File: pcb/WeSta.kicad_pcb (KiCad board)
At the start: 2 copper layers, 30 x 90 mm, 20 parts, among them J2 Conn_01x02, J3 RG-9/11/15, U1 ESP32-C3-MINI-1, U2 AW32001ECSR, U3 BH1730FVC, U4 BME280

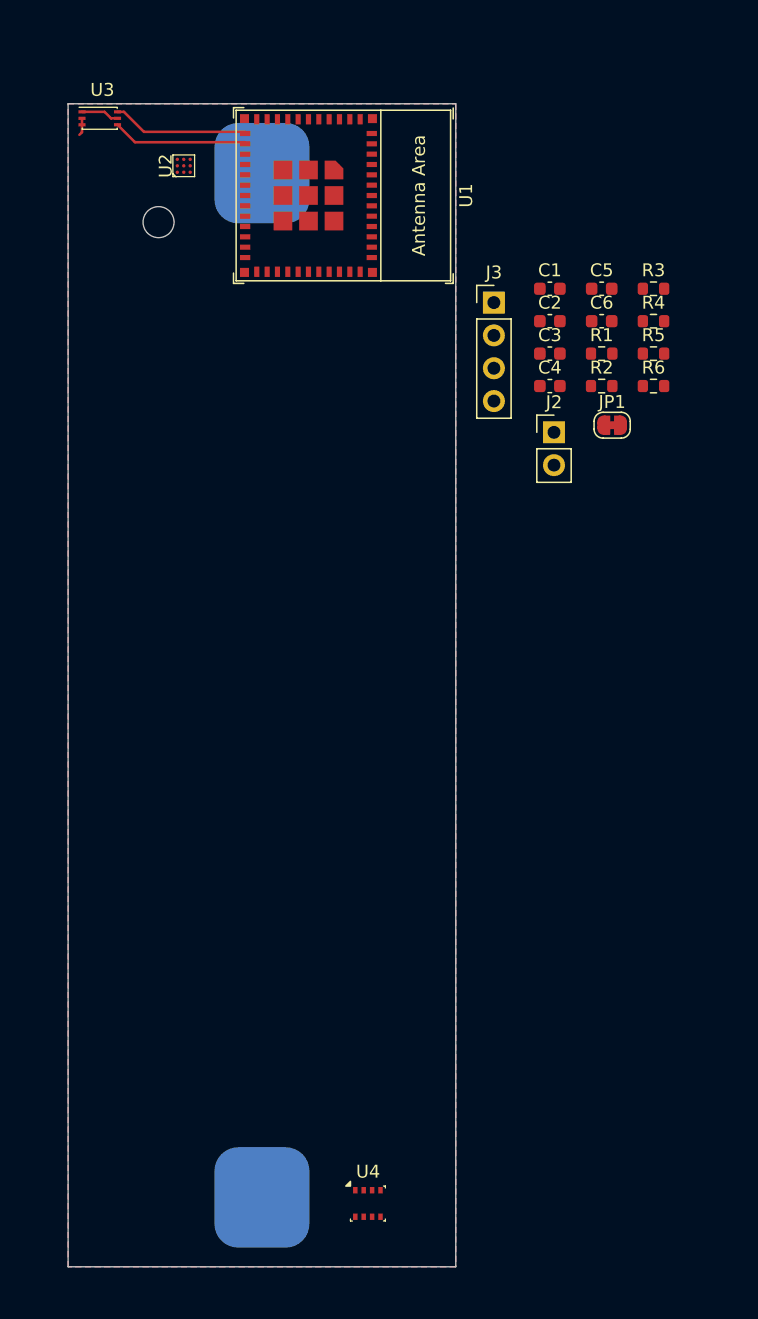
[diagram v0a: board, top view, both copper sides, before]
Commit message: Finalize rough PCB version
- Split sensors into own sub schematic as well as sub-sub sensor schematics
- Split piwer into own sub schematic
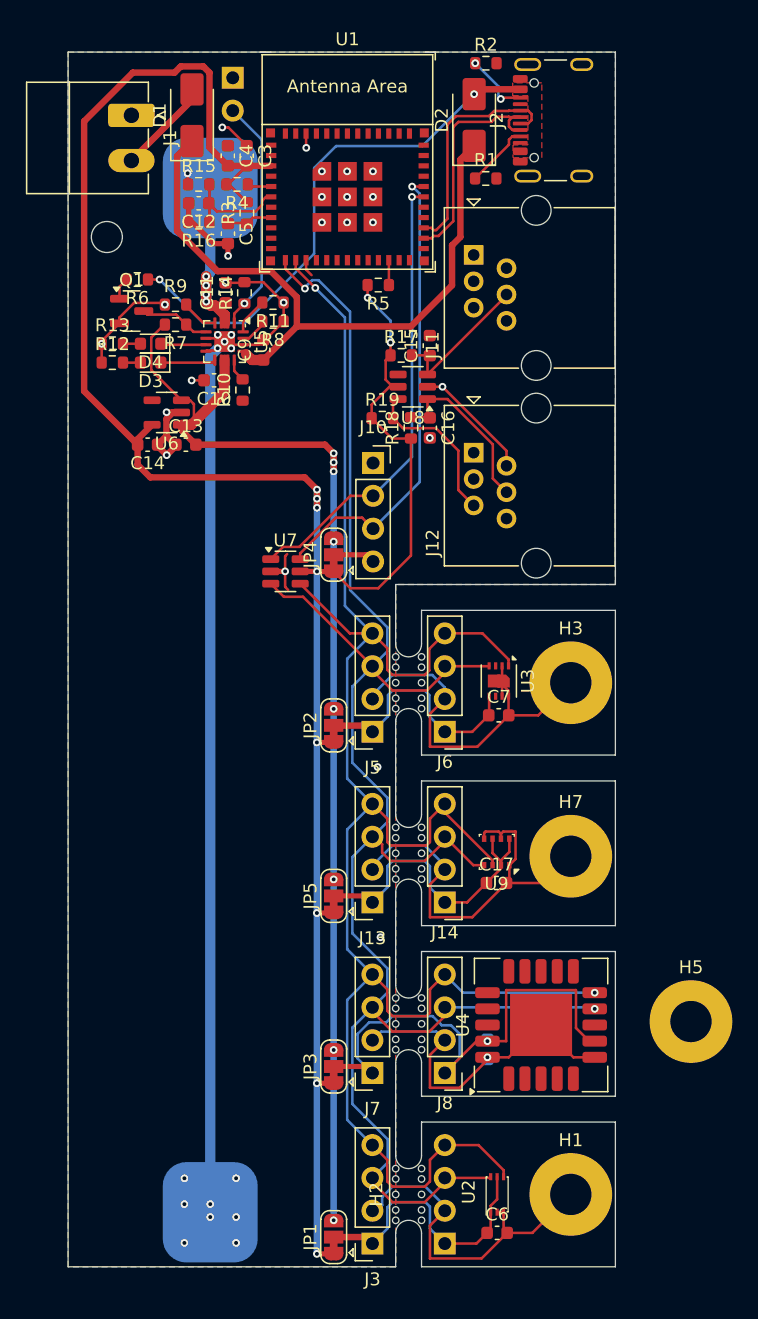
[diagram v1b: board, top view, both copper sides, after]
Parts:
- removed the C4 at (37.3, 21.8)
- removed the R4 at (45.3, 16.8)
- removed the R5 at (45.3, 19.3)
- added C10: 20u, Capacitor_SMD:C_0603_1608Metric, F.Cu at (11.3, 21.4)
- added C12: 100n, Capacitor_SMD:C_0603_1608Metric, F.Cu at (10.1, 7.70)
- added C13: 20u, Capacitor_SMD:C_0603_1608Metric, F.Cu at (9.12, 26.4)
- added C14: 20u, Capacitor_SMD:C_0603_1608Metric, F.Cu at (6.16, 26.4)
- added C15: 10p, Capacitor_SMD:C_0603_1608Metric, F.Cu at (28.0, 18.7)
- added C16: 10p, Capacitor_SMD:C_0603_1608Metric, F.Cu at (28.0, 25.1)
- added C17: 20u, Capacitor_SMD:C_0603_1608Metric, F.Cu at (33.1, 60.3)
- added C6: 20u, Capacitor_SMD:C_0603_1608Metric, F.Cu at (33.2, 87.4)
- added C7: 20u, Capacitor_SMD:C_0603_1608Metric, F.Cu at (33.3, 47.3)
- added C8: 20u, Capacitor_SMD:C_0603_1608Metric, B.Cu at (32.5, 73.2)
- added D1: SS34, Diode_SMD:D_SMA, F.Cu at (9.59, 0.89)
- added D2: SS34, Diode_SMD:D_SMA, F.Cu at (31.4, 1.26)
- added D3: chg, LED_SMD:LED_0603_1608Metric, F.Cu at (6.38, 20.0)
- added D4: pgood, LED_SMD:LED_0603_1608Metric, F.Cu at (6.38, 18.6)
- added H1: MountingHole_Pad, MountingHole:MountingHole_3.2mm_M3_Pad, F.Cu at (38.9, 84.4)
- added H2: mouse bites, panelization:mouse-bite-3mm-slot, F.Cu at (26.4, 84.4)
- added H3: MountingHole_Pad, MountingHole:MountingHole_3.2mm_M3_Pad, F.Cu at (38.9, 44.8)
- added H4: mouse bites, panelization:mouse-bite-3mm-slot, F.Cu at (26.4, 44.8)
- added H5: MountingHole_Pad, MountingHole:MountingHole_3.2mm_M3_Pad, F.Cu at (48.2, 71.0)
- added H6: mouse bites, panelization:mouse-bite-3mm-slot, F.Cu at (26.4, 71.2)
- added H7: MountingHole_Pad, MountingHole:MountingHole_3.2mm_M3_Pad, F.Cu at (38.9, 58.2)
- added H8: mouse bites, panelization:mouse-bite-3mm-slot, F.Cu at (26.4, 58.0)
- added J1: solar, Connector_Phoenix_MC:PhoenixContact_MC_1,5_2-G-3.5_1x02_P3.50mm_Horizontal, F.Cu at (4.90, 0.90)
- added J11: RJ12 (rain), Connector_RJ:RJ25_Wayconn_MJEA-660X1_Horizontal, F.Cu at (31.4, 11.7)
- added J12: RJ12 (wind), Connector_RJ:RJ25_Wayconn_MJEA-660X1_Horizontal, F.Cu at (31.4, 27.0)
- added J13: I2C Board, Connector_PinSocket_2.54mm:PinSocket_1x04_P2.54mm_Vertical, F.Cu at (23.6, 61.8)
- added J14: I2C Sensor, Connector_PinHeader_2.54mm:PinHeader_1x04_P2.54mm_Vertical, F.Cu at (29.1, 61.8)
- added J2: USB_C_Receptacle_USB2.0_16P, Connector_USB:USB_C_Receptacle_GCT_USB4105-xx-A_16P_TopMnt_Horizontal, F.Cu at (38.7, 1.28)
- added J3: I2C Board, Connector_PinSocket_2.54mm:PinSocket_1x04_P2.54mm_Vertical, F.Cu at (23.6, 88.2)
- added J4: I2C Sensor, Connector_PinHeader_2.54mm:PinHeader_1x04_P2.54mm_Vertical, B.Cu at (29.1, 88.2)
- added J5: I2C Board, Connector_PinSocket_2.54mm:PinSocket_1x04_P2.54mm_Vertical, F.Cu at (23.6, 48.6)
- added J6: I2C Sensor, Connector_PinHeader_2.54mm:PinHeader_1x04_P2.54mm_Vertical, F.Cu at (29.1, 48.6)
- added J7: I2C Board, Connector_PinSocket_2.54mm:PinSocket_1x04_P2.54mm_Vertical, F.Cu at (23.6, 75.0)
- added J8: I2C Sensor, Connector_PinHeader_2.54mm:PinHeader_1x04_P2.54mm_Vertical, F.Cu at (29.1, 75.0)
- added JP2: V select, Jumper:SolderJumper-3_P1.3mm_Bridged12_RoundedPad1.0x1.5mm, F.Cu at (20.6, 48.1)
- added JP3: V select, Jumper:SolderJumper-3_P1.3mm_Bridged12_RoundedPad1.0x1.5mm, F.Cu at (20.6, 74.5)
- added JP4: V select, Jumper:SolderJumper-3_P1.3mm_Bridged12_RoundedPad1.0x1.5mm, F.Cu at (20.6, 34.9)
- added JP5: V select, Jumper:SolderJumper-3_P1.3mm_Bridged12_RoundedPad1.0x1.5mm, F.Cu at (20.6, 61.3)
- added Q1: MOT S8050/J3Y/0.4, Package_TO_SOT_SMD:SOT-23, F.Cu at (4.92, 16.0)
- added R1: 5.1k, Resistor_SMD:R_0603_1608Metric, F.Cu at (32.3, 5.78)
- added R10: 1k (1.5A), Resistor_SMD:R_0603_1608Metric, F.Cu at (13.5, 22.1)
- added R11: 2k (0.5A), Resistor_SMD:R_0603_1608Metric, F.Cu at (15.9, 15.4)
- added R12: 10k, Resistor_SMD:R_0603_1608Metric, F.Cu at (3.42, 20.0)
- added R13: 10k, Resistor_SMD:R_0603_1608Metric, F.Cu at (3.42, 18.6)
- added R14: 10k, Resistor_SMD:R_0603_1608Metric, F.Cu at (13.6, 14.6)
- added R15: 470k, Resistor_SMD:R_0603_1608Metric, F.Cu at (10.1, 6.24)
- added R16: 470k, Resistor_SMD:R_0603_1608Metric, F.Cu at (10.1, 9.16)
- added R17: 100k, Resistor_SMD:R_0603_1608Metric, F.Cu at (25.8, 19.5)
- added R18: 10k, Resistor_SMD:R_0603_1608Metric, F.Cu at (26.5, 25.1)
- added R19: 10k, Resistor_SMD:R_0603_1608Metric, F.Cu at (24.3, 24.3)
- added R2: 5.1k, Resistor_SMD:R_0603_1608Metric, F.Cu at (32.3, -3.14)
- added R7: 100k, Resistor_SMD:R_0603_1608Metric, F.Cu at (8.31, 17.1)
- added R8: 10k (0.15A), Resistor_SMD:R_0603_1608Metric, F.Cu at (15.9, 16.8)
- added R9: 10k, Resistor_SMD:R_0603_1608Metric, F.Cu at (8.31, 15.5)
- added U4: SCD40-D-R2, Sensor:Sensirion_SCD4x-1EP_10.1x10.1mm_P1.25mm_EP4.8x4.8mm, F.Cu at (36.6, 71.3)
- added U5: BQ24074RGT, Package_DFN_QFN:VQFN-16-1EP_3x3mm_P0.5mm_EP1.6x1.6mm, F.Cu at (12.1, 18.4)
- added U6: RT9167A-33GB, Package_TO_SOT_SMD:TSOT-23-5, F.Cu at (7.63, 23.9)
- added U7: SRV05-4, Package_TO_SOT_SMD:SOT-23-6, F.Cu at (16.8, 36.2)
- added U8: SRV05-4, Package_TO_SOT_SMD:SOT-23-6, F.Cu at (26.7, 21.9)
- J10: renamed from J3; footprint Connector_PinHeader_2.54mm:PinHeader_1x04_P2.54mm_Vertical -> Connector_PinSocket_2.54mm:PinSocket_1x04_P2.54mm_Vertical
- J9: renamed from J2; moved to B.Cu
- JP1: value NTC -> V select; footprint Jumper:SolderJumper-2_P1.3mm_Bridged_RoundedPad1.0x1.5mm -> Jumper:SolderJumper-3_P1.3mm_Bridged12_RoundedPad1.0x1.5mm
- R6: value 10k -> 1k
- U2: value AW32001ECSR -> BH1730FVC; footprint wirmo_power:AW32001ECSR -> sensors:WSOF6
- U3: value BH1730FVC -> SHT31-DIS; footprint sensors:WSOF6 -> Sensor_Humidity:Sensirion_DFN-8-1EP_2.5x2.5mm_P0.5mm_EP1.1x1.7mm
- moved U2 83.2 mm to (33.2, 84.4)
- moved JP1 66.4 mm to (20.6, 87.7), turned to 90 degrees
- moved U3 53.4 mm to (33.3, 44.7), turned to -90 degrees
- moved R6 40.8 mm to (5.36, 13.6), turned to 180 degrees
- moved J9 37.0 mm to (12.7, -2.01), turned to 180 degrees
- moved R4 32.2 mm to (13.1, 6.24), turned to 180 degrees
- moved R3 32.0 mm to (13.8, 8.45), turned to 90 degrees
- moved C4 29.2 mm to (12.4, 4.03), turned to -90 degrees
- moved C11 29.2 mm to (12.2, 14.6), turned to 90 degrees
- moved U9 29.0 mm to (33.2, 57.9), turned to 180 degrees
- moved C3 26.7 mm to (13.8, 4.03), turned to -90 degrees
- moved C9 26.6 mm to (15.1, 19.1), turned to 90 degrees
- moved C5 25.3 mm to (12.4, 10.1), turned to -90 degrees
- moved R5 18.1 mm to (24.0, 14.0), turned to 180 degrees
- moved J10 15.5 mm to (23.6, 27.8)
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- renumbered C6 to C11, C2 to C3, C3 to C4, C1 to C5, C5 to C9, R2 to R4, R1 to R5, U4 to U9
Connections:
- C9 pad 1: +5V -> VBUS
- J10 pad 4: +5V -> Net-(J10-Pin_4)
- J9 pad 2: NTC -> Net-(J9-Pin_2)
- JP1 pad 1: VDD -> +3V3
- JP1 pad 2: NTC -> /sensors/BH1730/VCC
- R6 pad 1: VDD -> VUSB
- R6 pad 2: Int -> Net-(Q1-B)
- U1 pad 6: unconnected-(U1-GPIO3/ADC1_CH3-Pad6) -> IO3
- U3 pad 1: +3V3 -> SDA
- U3 pad 3: GND -> unconnected-(U3-ALERT-Pad3)
- U3 pad 4: SDA -> SCL
- U3 pad 5: +3V3 -> /sensors/HT31/VCC
- U3 pad 6: SCL -> unconnected-(U3-~{RESET}-Pad6)
- U9 pad 2: +3V3 -> VCC
- U9 pad 6: +3V3 -> VCC
- U9 pad 8: +3V3 -> VCC
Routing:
- net GND: track 1.36 -> 240.7 mm, vias 0 -> 38
- net +3V3: track 2.96 -> 177.1 mm, vias 0 -> 10
- net SDA: track 10.4 -> 154.6 mm, vias 0 -> 2
- net SCL: track 10.5 -> 148.7 mm, vias 0 -> 2
- net +5V: track 0.00 -> 91.4 mm, vias 0 -> 8
- net VBUS: track 0.00 -> 51.1 mm
- net VUSB: track 0.00 -> 41.6 mm, vias 0 -> 2
- net /sensors/SCD40/VCC: track 0.00 -> 39.3 mm, vias 0 -> 1
- net TX: track 0.00 -> 36.7 mm, vias 0 -> 1
- net RX: track 0.00 -> 35.2 mm, vias 0 -> 1
- net VCC: track 0.00 -> 23.7 mm
- net /sensors/BH1730/VCC: track 0.00 -> 21.0 mm
- net +BATT: track 0.00 -> 18.4 mm, vias 0 -> 5
- net Net-(J9-Pin_2): track 0.00 -> 18.2 mm, vias 0 -> 1
- net /sensors/HT31/VCC: track 0.00 -> 18.1 mm
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- added copper zone on B.Cu, net GND
- added copper zone on F.Cu, net VUSB
- removed copper zone on B.Cu, net +3V3
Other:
- board size 30 x 90 mm -> 42.4 x 94 mm
- board text added: "ADD USB RESISTORS"
